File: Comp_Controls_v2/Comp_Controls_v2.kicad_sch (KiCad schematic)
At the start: 0 parts

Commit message: Add 5V and 3.3V connectors, fix pin definitions
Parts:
- added 3.3V_SYS1: Conn_02x02_Counter_Clockwise, Connector_Molex:Molex_Mini-Fit_Jr_5566-04A_2x02_P4.20mm_Vertical, symbol Connector_Generic:Conn_02x02_Counter_Clockwise
- added 5V_SYS1: Conn_02x03_Counter_Clockwise, Connector_Molex:Molex_Mini-Fit_Jr_5566-06A_2x03_P4.20mm_Vertical, symbol Connector_Generic:Conn_02x03_Counter_Clockwise
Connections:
- new net +3.3V_SYS: 3.3V_SYS1.2 (Pin_2), 3.3V_SYS1.4 (Pin_4)
- new net +5V_SYS1: 5V_SYS1.1 (Pin_1), 5V_SYS1.2 (Pin_2), 5V_SYS1.3 (Pin_3)
- new net GND: 3.3V_SYS1.1 (Pin_1), 3.3V_SYS1.3 (Pin_3), 5V_SYS1.4 (Pin_4), 5V_SYS1.5 (Pin_5), 5V_SYS1.6 (Pin_6)

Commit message: save and redo commit
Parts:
- added C16, C17, C18: 0.1µF, ElectronicsFootprints:CAP_CL10B_01uf_0603, symbol Device:C
- added JIB4, SAIL3, TAIL3: B3B-XH-A, ElectronicsFootprints:B3B-XH-A, symbol 3-PinConnector:B3B-XH-A
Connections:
- net +5V_SYS1: now also C16.1, C17.1, JIB4.2, SAIL3.2
- net GND: now also C16.2, C17.2, C18.2, JIB4.3, SAIL3.3, TAIL3.3
- new net +5V_SYS2: C18.1, TAIL3.2
- new net JIB1: JIB4.1
- new net Sail: SAIL3.1
- new net Tail: TAIL3.1

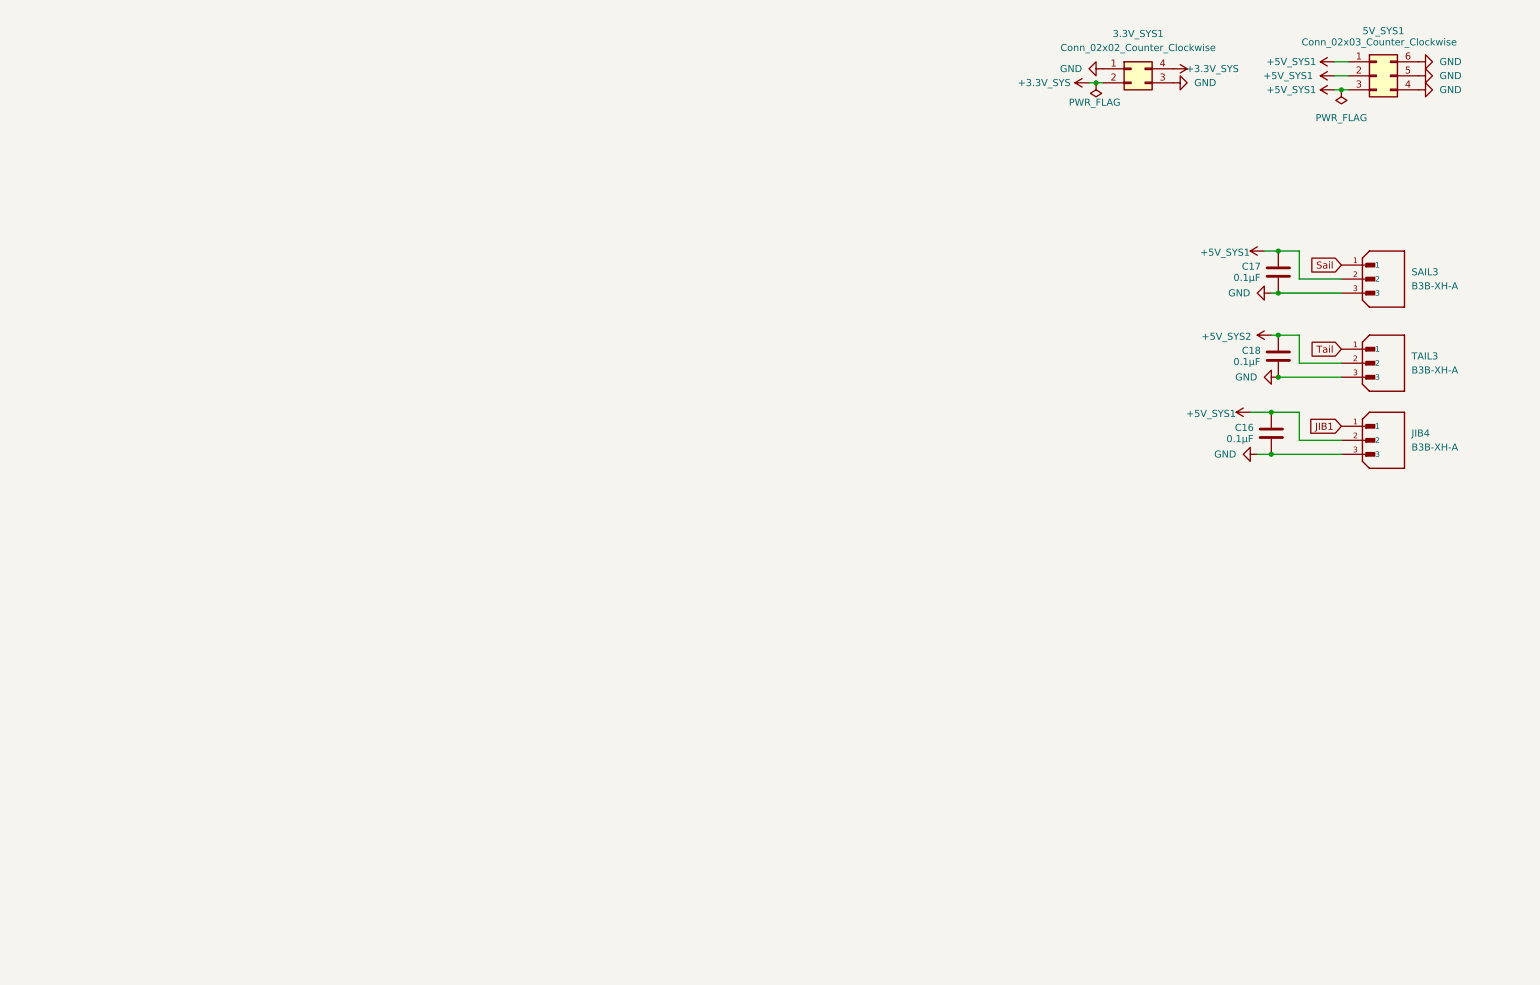
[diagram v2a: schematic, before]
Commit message: import parts from electronics PCB and fix DRC errors
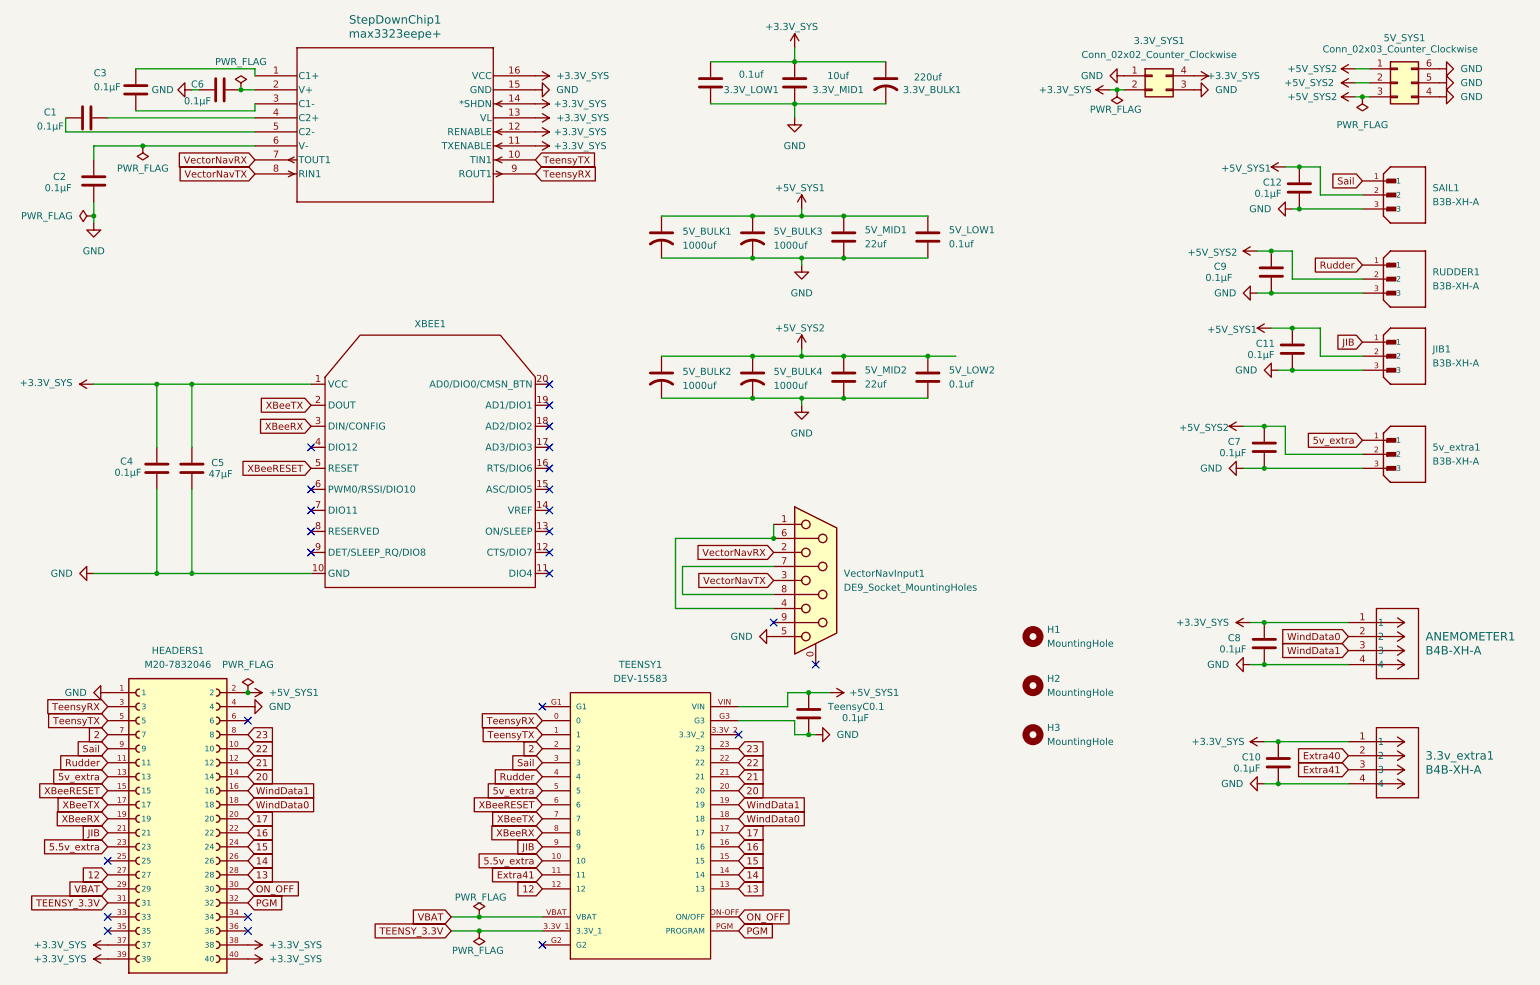
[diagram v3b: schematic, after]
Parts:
- added 3.3V_BULK1: 220uf, ElectronicsFootprints:CAP_87510_220uf, symbol Device:C_US
- added 3.3V_LOW1, 5V_LOW1, 5V_LOW2: 0.1uf, ElectronicsFootprints:CAP_CL10B_01uf_0603, symbol Device:C
- added 3.3V_MID1: 10uf, ElectronicsFootprints:CAP_CL21A_10uf_0805, symbol Device:C
- added 3.3v_extra1, ANEMOMETER1: B4B-XH-A, ElectronicsFootprints:B4B-XH-A, symbol 4-PinConnector:B4B-XH-A
- added 5V_BULK1, 5V_BULK2, 5V_BULK3, 5V_BULK4: 1000uf, ElectronicsFootprints:CAP_EEE1A_1000uf, symbol Device:C_US
- added 5V_MID1, 5V_MID2: 22uf, ElectronicsFootprints:CAP_CL32A_22uf_1210, symbol Device:C
- added 5v_extra1: B3B-XH-A, ElectronicsFootprints:B3B-XH-A, symbol 3-PinConnector:B3B-XH-A
- added C1, C10, C2, C3, C4, C6, C7, C8, TeensyC0.1: 0.1µF, ElectronicsFootprints:CAP_CL10B_01uf_0603, symbol Device:C
- added C5: 47µF, ElectronicsFootprints:CAP_C3225_47uf_1210, symbol Device:C
- added H1, H2, H3: MountingHole, MountingHole:MountingHole_3.2mm_M3, symbol Mechanical:MountingHole
- added HEADERS1: M20-7832046, ElectronicsFootprints:HARWIN_M20-7832046, symbol TeensyConnector:M20-7832046
- added StepDownChip1: max3323eepe+, ElectronicsFootprints:MAX3323EEPE+, symbol VectorNav2:max3323eepe+
- added TEENSY1: DEV-15583, ElectronicsFootprints:MODULE_DEV-15583, symbol Teensy:DEV-15583
- added VectorNavInput1: DE9_Socket_MountingHoles, Connector_Dsub:DSUB-9_Socket_Vertical_P2.77x2.84mm_MountingHoles, symbol Connector:DE9_Socket_MountingHoles
- added XBEE1: ~, ElectronicsFootprints:XBee, symbol VectorNav2:Xbee_pro_s3b
- renumbered C16 to C11, C17 to C12, C18 to C9, JIB4 to JIB1, TAIL3 to RUDDER1, SAIL3 to SAIL1
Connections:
- net +3.3V_SYS: now also 3.3V_BULK1.1, 3.3V_LOW1.1, 3.3V_MID1.1, 3.3v_extra1.1, ANEMOMETER1.1, C10.1, C4.1, C5.1, C8.1, HEADERS1.37, HEADERS1.38, HEADERS1.39, HEADERS1.40, StepDownChip1.11 (TXENABLE), StepDownChip1.12 (RENABLE), StepDownChip1.13 (VL), StepDownChip1.14 (*SHDN), StepDownChip1.16 (VCC), XBEE1.1 (VCC)
- net +5V_SYS1: now also 5V_BULK1.1, 5V_BULK3.1, 5V_LOW1.2, 5V_MID1.2, HEADERS1.2, TEENSY1.VIN, TeensyC0.1.2; no longer 5V_SYS1.1 (Pin_1), 5V_SYS1.2 (Pin_2), 5V_SYS1.3 (Pin_3)
- net +5V_SYS2: now also 5V_SYS1.1 (Pin_1), 5V_SYS1.2 (Pin_2), 5V_SYS1.3 (Pin_3), 5V_BULK2.1, 5V_BULK4.1, 5V_LOW2.2, 5V_MID2.2, 5v_extra1.2, C7.1
- net GND: now also 3.3V_BULK1.2, 3.3V_LOW1.2, 3.3V_MID1.2, 3.3v_extra1.4, 5V_BULK1.2, 5V_BULK2.2, 5V_BULK3.2, 5V_BULK4.2, 5V_LOW1.1, 5V_LOW2.1, 5V_MID1.1, 5V_MID2.1, 5v_extra1.3, ANEMOMETER1.4, C10.2, C2.2, C4.2, C5.2, C6.1, C7.2, C8.2, HEADERS1.1, HEADERS1.4, StepDownChip1.15 (GND), TEENSY1.G3, TeensyC0.1.1, VectorNavInput1.5, XBEE1.10 (GND)
- net Sail: now also HEADERS1.9, TEENSY1.3
- net JIB1 renamed JIB
- net JIB: now also HEADERS1.21, TEENSY1.9
- net Tail renamed Rudder
- net Rudder: now also HEADERS1.11, TEENSY1.4
- new net: C6.2, StepDownChip1.2 (V+)
- new net: C3.1, StepDownChip1.1 (C1+)
- new net: C3.2, StepDownChip1.3 (C1-)
- new net: C2.1, StepDownChip1.6 (V-)
- new net: VectorNavInput1.1, VectorNavInput1.4, VectorNavInput1.6
- new net: VectorNavInput1.7, VectorNavInput1.8
- new net: C1.1, StepDownChip1.4 (C2+)
- new net: C1.2, StepDownChip1.5 (C2-)
- new net 12: HEADERS1.27, TEENSY1.12
- new net 13: HEADERS1.28, TEENSY1.13
- new net 14: HEADERS1.26, TEENSY1.14
- new net 15: HEADERS1.24, TEENSY1.15
- new net 16: HEADERS1.22, TEENSY1.16
- new net 17: HEADERS1.20, TEENSY1.17
- new net 2: HEADERS1.7, TEENSY1.2
- new net 20: HEADERS1.14, TEENSY1.20
- new net 21: HEADERS1.12, TEENSY1.21
- new net 22: HEADERS1.10, TEENSY1.22
- new net 23: HEADERS1.8, TEENSY1.23
- new net 5.5v_extra: HEADERS1.23, TEENSY1.10
- new net 5v_extra: 5v_extra1.1, HEADERS1.13, TEENSY1.5
- new net Extra40: 3.3v_extra1.2
- new net Extra41: 3.3v_extra1.3, TEENSY1.11
- new net ON_OFF: HEADERS1.30, TEENSY1.ON-OFF (ON/OFF)
- new net PGM: HEADERS1.32, TEENSY1.PGM (PROGRAM)
- new net TEENSY_3.3V: HEADERS1.31, TEENSY1.3.3V_1
- new net TeensyRX: HEADERS1.3, StepDownChip1.9 (ROUT1), TEENSY1.0
- new net TeensyTX: HEADERS1.5, StepDownChip1.10 (TIN1), TEENSY1.1
- new net VBAT: HEADERS1.29, TEENSY1.VBAT
- new net VectorNavRX: StepDownChip1.7 (TOUT1), VectorNavInput1.2
- new net VectorNavTX: StepDownChip1.8 (RIN1), VectorNavInput1.3
- new net WindData0: ANEMOMETER1.2, HEADERS1.18, TEENSY1.18
- new net WindData1: ANEMOMETER1.3, HEADERS1.16, TEENSY1.19
- new net XBeeRESET: HEADERS1.15, TEENSY1.6, XBEE1.5 (RESET)
- new net XBeeRX: HEADERS1.19, TEENSY1.8, XBEE1.3 (DIN/CONFIG)
- new net XBeeTX: HEADERS1.17, TEENSY1.7, XBEE1.2 (DOUT)
- no-connect marks 0 -> 26
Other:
- moved on the sheet: 3.3V_SYS1, 5V_SYS1, C11, C12, C9, JIB1, RUDDER1, SAIL1

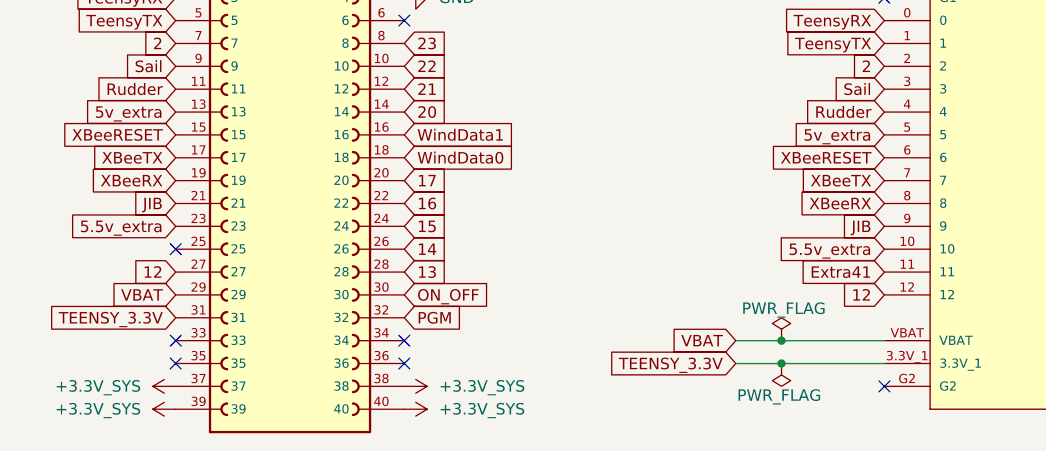
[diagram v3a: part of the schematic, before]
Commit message: resolve all unspecified pin errors
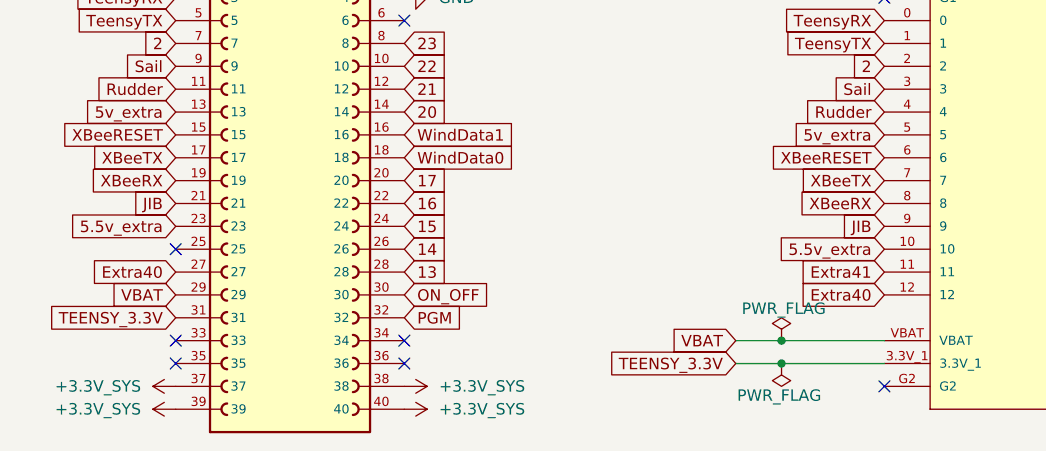
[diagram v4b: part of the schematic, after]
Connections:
- net 12 is gone; now on net Extra40: HEADERS1.27, TEENSY1.12
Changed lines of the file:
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@@
 		)
 	)
-	(global_label "12"
+	(global_label "Extra40"
 		(shape input)
 		(at 29.21 173.99 180)
@@
 		)
 		(property "Intersheetrefs" "${INTERSHEET_REFS}"
-			(at 23.8058 173.99 0)
+			(at 18.9678 173.99 0)
 			(effects
 				(font
@@
 		)
 	)
-	(global_label "12"
+	(global_label "Extra40"
 		(shape input)
 		(at 107.95 176.53 180)
@@
 		)
 		(property "Intersheetrefs" "${INTERSHEET_REFS}"
-			(at 102.5458 176.53 0)
+			(at 97.7078 176.53 0)
 			(effects
 				(font
@@
 	)
 	(symbol
+		(lib_name "B4B-XH-A_1")
 		(lib_id "4-PinConnector:B4B-XH-A")
 		(at 254 149.86 0)
